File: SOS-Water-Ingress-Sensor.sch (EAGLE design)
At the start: 1 part

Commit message: Update board design and schematic.
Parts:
- added JP1: (no value), SparkFun-Connectors:M03PTH
- added Q1: (no value), SparkFun-DiscreteSemi:TRANSISTOR_PNPSMD
- added R1, R3: 10K, resistor:R-US_R0603
- added R2: 200K, resistor:R-US_R0603
- added U$1, U$2, U$3, U$4: JSH-GH-2VERT, BlueRobotics-JST-GH:JSH-GH-2VERT
- added U$5: JST-GH-3VERT, BlueRobotics-JST-GH:JST-GH-3VERT
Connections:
- new net GND: JP1.1, R3.2, U$1.2, U$2.2, U$3.2, U$4.2
- new net N$1: Q1.B, R1.1, R2.1
- new net PROBE: R1.2, U$1.1, U$2.1, U$3.1, U$4.1
- new net SIGNAL: JP1.3, Q1.C, R3.1
- new net VCC: JP1.2, Q1.E, R2.2
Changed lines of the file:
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@@
 <part name="FRAME1" library="BlueRobotics-Main" deviceset="FRAME-BLUEROBOTICS" device=""/>
 <part name="U$7" library="BR-Eagle-Library" deviceset="LOGO" device="BR-LOGO-S" value="LOGOBR-LOGO-S"/>
+<part name="JP1" library="SparkFun-Connectors" deviceset="M03" device="PTH"/>
+<part name="P+1" library="supply1" deviceset="VCC" device=""/>
+<part name="GND1" library="supply1" deviceset="GND" device=""/>
+<part name="R2" library="resistor" deviceset="R-US_" device="R0603" value="200K"/>
+<part name="GND2" library="supply1" deviceset="GND" device=""/>
+<part name="R1" library="resistor" deviceset="R-US_" device="R0603" value="10K"/>
+<part name="P+2" library="supply1" deviceset="VCC" device=""/>
+<part name="U$1" library="BlueRobotics-JST-GH" deviceset="JSH-GH-2" device="VERT"/>
+<part name="Q1" library="SparkFun-DiscreteSemi" deviceset="TRANSISTOR_PNP" device="SMD"/>
+<part name="R3" library="resistor" deviceset="R-US_" device="R0603" value="10K"/>
+<part name="U$2" library="BlueRobotics-JST-GH" deviceset="JSH-GH-2" device="VERT"/>
+<part name="U$3" library="BlueRobotics-JST-GH" deviceset="JSH-GH-2" device="VERT"/>
+<part name="U$4" library="BlueRobotics-JST-GH" deviceset="JSH-GH-2" device="VERT"/>
+<part name="U$5" library="BlueRobotics-JST-GH" deviceset="JST-GH-3" device="VERT"/>
 </parts>
 <sheets>
@@
 </plain>
 <instances>
-<instance part="FRAME1" gate="G$1" x="-96.52" y="-88.9"/>
-<instance part="FRAME1" gate="G$2" x="50.8" y="-88.9"/>
-<instance part="U$7" gate="G$1" x="127" y="78.74"/>
+<instance part="FRAME1" gate="G$1" x="0" y="0"/>
+<instance part="FRAME1" gate="G$2" x="147.32" y="0"/>
+<instance part="U$7" gate="G$1" x="223.52" y="167.64"/>
+<instance part="JP1" gate="G$1" x="43.18" y="127"/>
+<instance part="P+1" gate="VCC" x="58.42" y="139.7"/>
+<instance part="GND1" gate="1" x="58.42" y="116.84"/>
+<instance part="R2" gate="G$1" x="119.38" y="111.76" rot="R90"/>
+<instance part="GND2" gate="1" x="132.08" y="78.74"/>
+<instance part="R1" gate="G$1" x="109.22" y="104.14" rot="R180"/>
+<instance part="P+2" gate="VCC" x="132.08" y="124.46"/>
+<instance part="U$1" gate="G$1" x="187.96" y="127"/>
+<instance part="Q1" gate="G$1" x="129.54" y="104.14"/>
+<instance part="R3" gate="G$1" x="132.08" y="88.9" rot="R270"/>
+<instance part="U$2" gate="G$1" x="187.96" y="114.3"/>
+<instance part="U$3" gate="G$1" x="187.96" y="101.6"/>
+<instance part="U$4" gate="G$1" x="187.96" y="88.9"/>
+<instance part="U$5" gate="G$1" x="45.72" y="106.68" rot="R180"/>
 </instances>
 <busses>
 </busses>
 <nets>
+<net name="VCC" class="0">
+<segment>
+<pinref part="P+1" gate="VCC" pin="VCC"/>
+<wire x1="58.42" y1="127" x2="58.42" y2="137.16" width="0.1524" layer="91"/>
+<pinref part="JP1" gate="G$1" pin="2"/>
+<wire x1="50.8" y1="127" x2="58.42" y2="127" width="0.1524" layer="91"/>
+</segment>
+<segment>
+<pinref part="P+2" gate="VCC" pin="VCC"/>
+<pinref part="R2" gate="G$1" pin="2"/>
+<wire x1="132.08" y1="119.38" x2="132.08" y2="121.92" width="0.1524" layer="91"/>
+<wire x1="119.38" y1="116.84" x2="119.38" y2="119.38" width="0.1524" layer="91"/>
+<wire x1="119.38" y1="119.38" x2="132.08" y2="119.38" width="0.1524" layer="91"/>
+<junction x="132.08" y="119.38"/>
+<pinref part="Q1" gate="G$1" pin="E"/>
+<wire x1="132.08" y1="109.22" x2="132.08" y2="119.38" width="0.1524" layer="91"/>
+</segment>
+</net>
+<net name="GND" class="0">
+<segment>
+<pinref part="JP1" gate="G$1" pin="1"/>
+<pinref part="GND1" gate="1" pin="GND"/>
+<wire x1="50.8" y1="124.46" x2="58.42" y2="124.46" width="0.1524" layer="91"/>
+<wire x1="58.42" y1="124.46" x2="58.42" y2="119.38" width="0.1524" layer="91"/>
+</segment>
+<segment>
+<pinref part="U$1" gate="G$1" pin="2"/>
+<wire x1="182.88" y1="132.08" x2="180.34" y2="132.08" width="0.1524" layer="91"/>
+<label x="170.18" y="132.08" size="1.778" layer="95"/>
+<pinref part="U$4" gate="G$1" pin="2"/>
+<wire x1="180.34" y1="132.08" x2="170.18" y2="132.08" width="0.1524" layer="91"/>
+<wire x1="182.88" y1="93.98" x2="180.34" y2="93.98" width="0.1524" layer="91"/>
+<wire x1="180.34" y1="93.98" x2="180.34" y2="106.68" width="0.1524" layer="91"/>
+<junction x="180.34" y="132.08"/>
+<pinref part="U$2" gate="G$1" pin="2"/>
+<wire x1="180.34" y1="106.68" x2="180.34" y2="119.38" width="0.1524" layer="91"/>
+<wire x1="180.34" y1="119.38" x2="180.34" y2="132.08" width="0.1524" layer="91"/>
+<wire x1="182.88" y1="119.38" x2="180.34" y2="119.38" width="0.1524" layer="91"/>
+<junction x="180.34" y="119.38"/>
+<pinref part="U$3" gate="G$1" pin="2"/>
+<wire x1="182.88" y1="106.68" x2="180.34" y2="106.68" width="0.1524" layer="91"/>
+<junction x="180.34" y="106.68"/>
+</segment>
+<segment>
+<pinref part="GND2" gate="1" pin="GND"/>
+<pinref part="R3" gate="G$1" pin="2"/>
+<wire x1="132.08" y1="81.28" x2="132.08" y2="83.82" width="0.1524" layer="91"/>
+</segment>
+</net>
+<net name="SIGNAL" class="0">
+<segment>
+<pinref part="JP1" gate="G$1" pin="3"/>
+<wire x1="50.8" y1="129.54" x2="71.12" y2="129.54" width="0.1524" layer="91"/>
+<label x="60.96" y="129.54" size="1.778" layer="95"/>
+</segment>
+<segment>
+<pinref part="Q1" gate="G$1" pin="C"/>
+<pinref part="R3" gate="G$1" pin="1"/>
+<wire x1="132.08" y1="93.98" x2="132.08" y2="96.52" width="0.1524" layer="91"/>
+<wire x1="132.08" y1="96.52" x2="132.08" y2="99.06" width="0.1524" layer="91"/>
+<wire x1="132.08" y1="96.52" x2="147.32" y2="96.52" width="0.1524" layer="91"/>
+<junction x="132.08" y="96.52"/>
+<label x="139.7" y="96.52" size="1.778" layer="95"/>
+</segment>
+</net>
+<net name="N$1" class="0">
+<segment>
+<wire x1="114.3" y1="104.14" x2="119.38" y2="104.14" width="0.1524" layer="91"/>
+<pinref part="R1" gate="G$1" pin="1"/>
+<pinref part="Q1" gate="G$1" pin="B"/>
+<pinref part="R2" gate="G$1" pin="1"/>
+<wire x1="119.38" y1="104.14" x2="127" y2="104.14" width="0.1524" layer="91"/>
+<wire x1="119.38" y1="106.68" x2="119.38" y2="104.14" width="0.1524" layer="91"/>
+<junction x="119.38" y="104.14"/>
+</segment>
+</net>
+<net name="PROBE" class="0">
+<segment>
+<pinref part="U$1" gate="G$1" pin="1"/>
+<wire x1="182.88" y1="129.54" x2="177.8" y2="129.54" width="0.1524" layer="91"/>
+<label x="170.18" y="129.54" size="1.778" layer="95"/>
+<pinref part="U$4" gate="G$1" pin="1"/>
+<wire x1="177.8" y1="129.54" x2="170.18" y2="129.54" width="0.1524" layer="91"/>
+<wire x1="182.88" y1="91.44" x2="177.8" y2="91.44" width="0.1524" layer="91"/>
+<wire x1="177.8" y1="91.44" x2="177.8" y2="104.14" width="0.1524" layer="91"/>
+<junction x="177.8" y="129.54"/>
+<pinref part="U$2" gate="G$1" pin="1"/>
+<wire x1="177.8" y1="104.14" x2="177.8" y2="116.84" width="0.1524" layer="91"/>
+<wire x1="177.8" y1="116.84" x2="177.8" y2="129.54" width="0.1524" layer="91"/>
+<wire x1="182.88" y1="116.84" x2="177.8" y2="116.84" width="0.1524" layer="91"/>
+<junction x="177.8" y="116.84"/>
+<pinref part="U$3" gate="G$1" pin="1"/>
+<wire x1="182.88" y1="104.14" x2="177.8" y2="104.14" width="0.1524" layer="91"/>
+<junction x="177.8" y="104.14"/>
+</segment>
+<segment>
+<pinref part="R1" gate="G$1" pin="2"/>
+<wire x1="104.14" y1="104.14" x2="93.98" y2="104.14" width="0.1524" layer="91"/>
+<label x="93.98" y="104.14" size="1.778" layer="95"/>
+</segment>
+</net>
 </nets>
 </sheet>

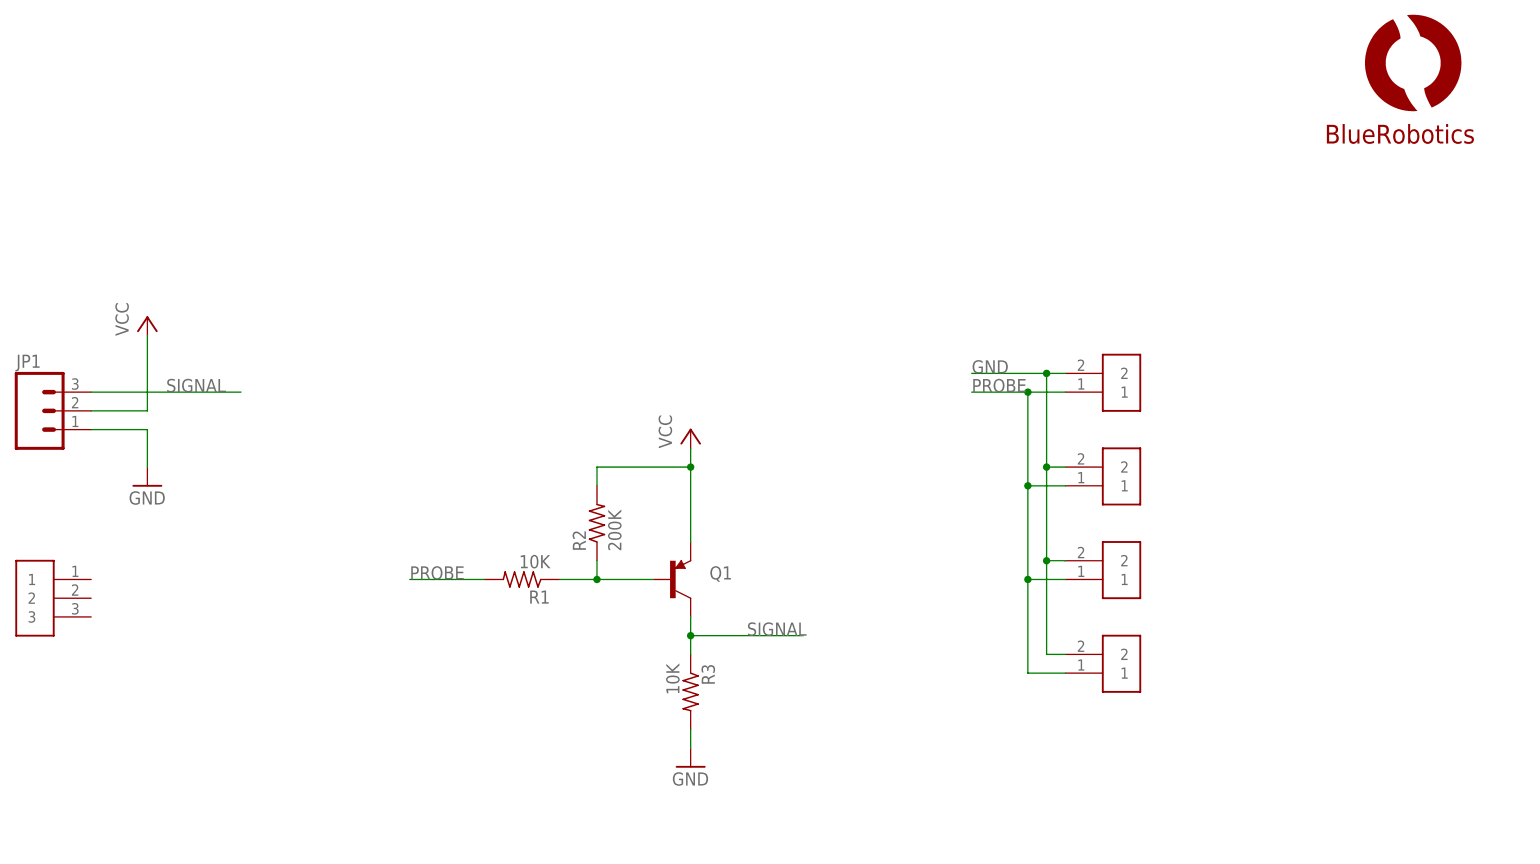
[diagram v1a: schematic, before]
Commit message: Added LED indicator and resistor, completed board layout.
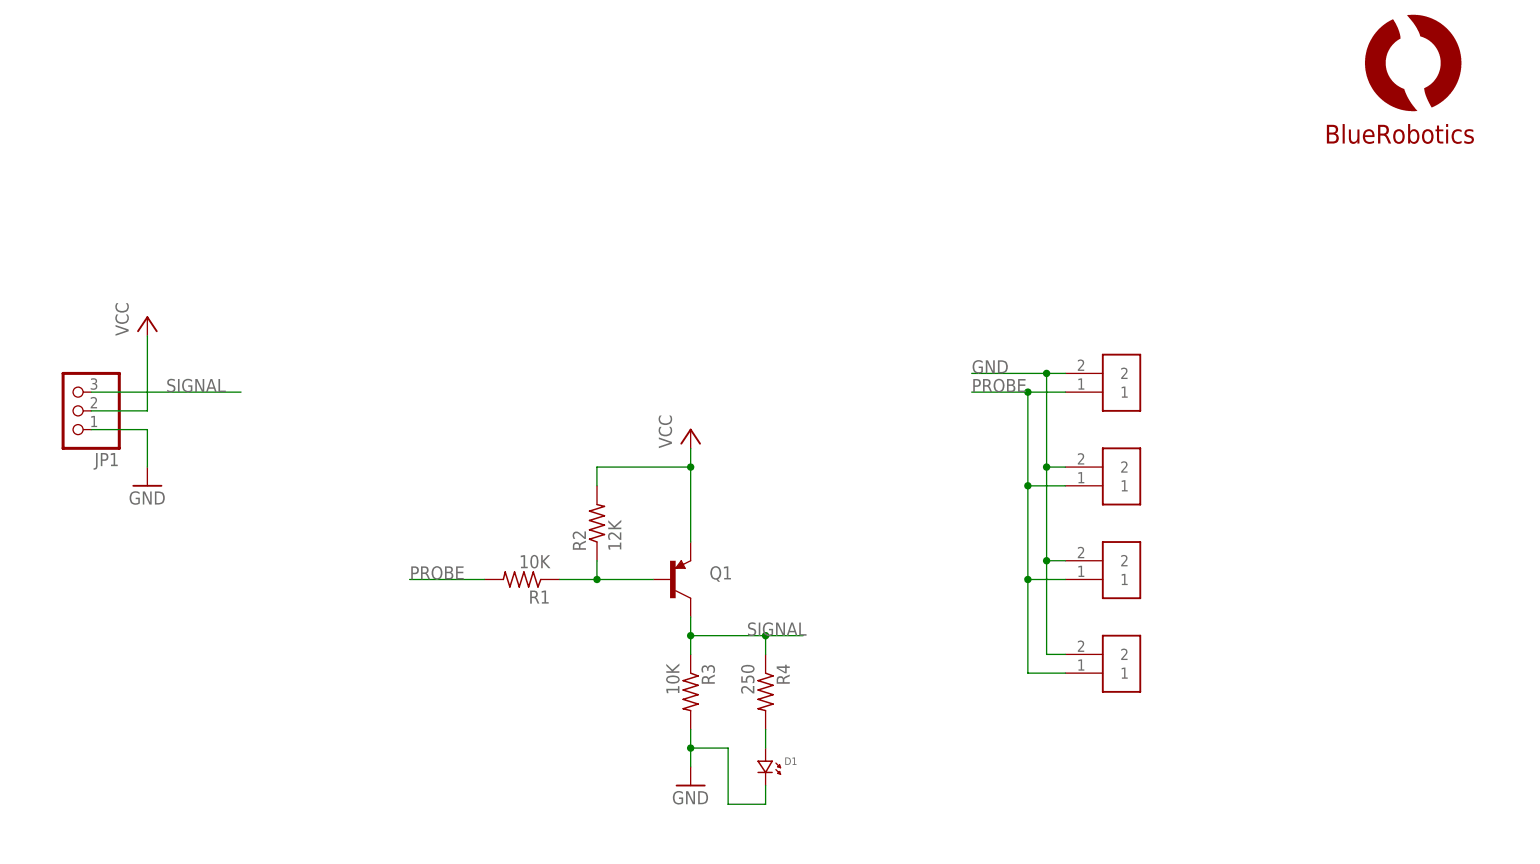
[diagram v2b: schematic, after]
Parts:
- removed U$5: JST-GH-3VERT, BlueRobotics-JST-GH:JST-GH-3VERT
- added D1: (no value), standardparts:LED.0805
- added R4: 250, resistor:R-US_R0603
- JP1: device SparkFun-Connectors:M03PTH -> pinhead+:PINHD-1X3
- R2: value 200K -> 12K
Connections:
- new net N$2: D1.1, R4.2
- net GND: now also D1.2
- net SIGNAL: now also R4.1
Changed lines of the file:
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@@
 <?xml version="1.0" encoding="utf-8"?>
 <!DOCTYPE eagle SYSTEM "eagle.dtd">
-<eagle version="7.4.0">
+<eagle version="7.6.0">
 <drawing>
 <settings>
@@
 <layer number="56" name="wert" color="7" fill="1" visible="no" active="no"/>
 <layer number="57" name="tCAD" color="7" fill="1" visible="no" active="no"/>
+<layer number="59" name="tCarbon" color="7" fill="1" visible="no" active="no"/>
+<layer number="60" name="bCarbon" color="7" fill="1" visible="no" active="no"/>
 <layer number="90" name="Modules" color="5" fill="1" visible="yes" active="yes"/>
 <layer number="91" name="Nets" color="2" fill="1" visible="yes" active="yes"/>
@@
 <layer number="127" name="_tValues" color="7" fill="1" visible="yes" active="yes"/>
 <layer number="128" name="_bValues" color="7" fill="1" visible="yes" active="yes"/>
+<layer number="129" name="Mask" color="7" fill="1" visible="yes" active="yes"/>
 <layer number="130" name="SMDSTROOK" color="7" fill="1" visible="yes" active="yes"/>
 <layer number="131" name="tAdjust" color="7" fill="1" visible="yes" active="yes"/>
@@
 <layer number="227" name="227bmp" color="7" fill="1" visible="yes" active="yes"/>
 <layer number="228" name="228bmp" color="7" fill="1" visible="yes" active="yes"/>
+<layer number="229" name="229bmp" color="7" fill="1" visible="yes" active="yes"/>
 <layer number="230" name="230bmp" color="7" fill="1" visible="yes" active="yes"/>
 <layer number="231" name="Eagle3D_PG1" color="7" fill="1" visible="yes" active="yes"/>
@@
 <part name="FRAME1" library="BlueRobotics-Main" deviceset="FRAME-BLUEROBOTICS" device=""/>
 <part name="U$7" library="BR-Eagle-Library" deviceset="LOGO" device="BR-LOGO-S" value="LOGOBR-LOGO-S"/>
-<part name="JP1" library="SparkFun-Connectors" deviceset="M03" device="PTH"/>
 <part name="P+1" library="supply1" deviceset="VCC" device=""/>
 <part name="GND1" library="supply1" deviceset="GND" device=""/>
-<part name="R2" library="resistor" deviceset="R-US_" device="R0603" value="200K"/>
+<part name="R2" library="resistor" deviceset="R-US_" device="R0603" value="12K"/>
 <part name="GND2" library="supply1" deviceset="GND" device=""/>
 <part name="R1" library="resistor" deviceset="R-US_" device="R0603" value="10K"/>
@@
 <part name="U$2" library="BlueRobotics-JST-GH" deviceset="JSH-GH-2" device="VERT"/>
 <part name="U$3" library="BlueRobotics-JST-GH" deviceset="JSH-GH-2" device="VERT"/>
+<part name="JP1" library="pinhead+" deviceset="PINHD-1X3" device=""/>
+<part name="R4" library="resistor" deviceset="R-US_" device="R0603" value="250"/>
+<part name="D1" library="standardparts" deviceset="LED" device=".0805"/>
 <part name="U$4" library="BlueRobotics-JST-GH" deviceset="JSH-GH-2" device="VERT"/>
-<part name="U$5" library="BlueRobotics-JST-GH" deviceset="JST-GH-3" device="VERT"/>
 </parts>
 <sheets>
@@
 <instance part="FRAME1" gate="G$2" x="147.32" y="0"/>
 <instance part="U$7" gate="G$1" x="223.52" y="167.64"/>
-<instance part="JP1" gate="G$1" x="43.18" y="127"/>
 <instance part="P+1" gate="VCC" x="58.42" y="139.7"/>
 <instance part="GND1" gate="1" x="58.42" y="116.84"/>
 <instance part="R2" gate="G$1" x="119.38" y="111.76" rot="R90"/>
-<instance part="GND2" gate="1" x="132.08" y="78.74"/>
+<instance part="GND2" gate="1" x="132.08" y="76.2"/>
 <instance part="R1" gate="G$1" x="109.22" y="104.14" rot="R180"/>
 <instance part="P+2" gate="VCC" x="132.08" y="124.46"/>
@@
 <instance part="U$2" gate="G$1" x="187.96" y="114.3"/>
 <instance part="U$3" gate="G$1" x="187.96" y="101.6"/>
+<instance part="JP1" gate="A" x="48.26" y="127" rot="R180"/>
+<instance part="R4" gate="G$1" x="142.24" y="88.9" rot="R270"/>
+<instance part="D1" gate="G$1" x="142.24" y="78.74" rot="R270"/>
 <instance part="U$4" gate="G$1" x="187.96" y="88.9"/>
-<instance part="U$5" gate="G$1" x="45.72" y="106.68" rot="R180"/>
 </instances>
 <busses>
@@
 <pinref part="P+1" gate="VCC" pin="VCC"/>
 <wire x1="58.42" y1="127" x2="58.42" y2="137.16" width="0.1524" layer="91"/>
-<pinref part="JP1" gate="G$1" pin="2"/>
 <wire x1="50.8" y1="127" x2="58.42" y2="127" width="0.1524" layer="91"/>
+<pinref part="JP1" gate="A" pin="2"/>
 </segment>
 <segment>
@@
 <net name="GND" class="0">
 <segment>
-<pinref part="JP1" gate="G$1" pin="1"/>
 <pinref part="GND1" gate="1" pin="GND"/>
 <wire x1="50.8" y1="124.46" x2="58.42" y2="124.46" width="0.1524" layer="91"/>
 <wire x1="58.42" y1="124.46" x2="58.42" y2="119.38" width="0.1524" layer="91"/>
+<pinref part="JP1" gate="A" pin="1"/>
 </segment>
 <segment>
@@
 <wire x1="182.88" y1="132.08" x2="180.34" y2="132.08" width="0.1524" layer="91"/>
 <label x="170.18" y="132.08" size="1.778" layer="95"/>
-<pinref part="U$4" gate="G$1" pin="2"/>
 <wire x1="180.34" y1="132.08" x2="170.18" y2="132.08" width="0.1524" layer="91"/>
-<wire x1="182.88" y1="93.98" x2="180.34" y2="93.98" width="0.1524" layer="91"/>
-<wire x1="180.34" y1="93.98" x2="180.34" y2="106.68" width="0.1524" layer="91"/>
 <junction x="180.34" y="132.08"/>
 <pinref part="U$2" gate="G$1" pin="2"/>
@@
 <pinref part="U$3" gate="G$1" pin="2"/>
 <wire x1="182.88" y1="106.68" x2="180.34" y2="106.68" width="0.1524" layer="91"/>
+<wire x1="180.34" y1="106.68" x2="180.34" y2="93.98" width="0.1524" layer="91"/>
 <junction x="180.34" y="106.68"/>
+<pinref part="U$4" gate="G$1" pin="2"/>
+<wire x1="180.34" y1="93.98" x2="182.88" y2="93.98" width="0.1524" layer="91"/>
 </segment>
 <segment>
 <pinref part="GND2" gate="1" pin="GND"/>
 <pinref part="R3" gate="G$1" pin="2"/>
+<wire x1="132.08" y1="78.74" x2="132.08" y2="81.28" width="0.1524" layer="91"/>
+<pinref part="D1" gate="G$1" pin="2"/>
 <wire x1="132.08" y1="81.28" x2="132.08" y2="83.82" width="0.1524" layer="91"/>
+<wire x1="142.24" y1="76.2" x2="142.24" y2="73.66" width="0.1524" layer="91"/>
+<wire x1="142.24" y1="73.66" x2="137.16" y2="73.66" width="0.1524" layer="91"/>
+<wire x1="137.16" y1="73.66" x2="137.16" y2="81.28" width="0.1524" layer="91"/>
+<wire x1="137.16" y1="81.28" x2="132.08" y2="81.28" width="0.1524" layer="91"/>
+<junction x="132.08" y="81.28"/>
 </segment>
 </net>
 <net name="SIGNAL" class="0">
 <segment>
-<pinref part="JP1" gate="G$1" pin="3"/>
 <wire x1="50.8" y1="129.54" x2="71.12" y2="129.54" width="0.1524" layer="91"/>
 <label x="60.96" y="129.54" size="1.778" layer="95"/>
+<pinref part="JP1" gate="A" pin="3"/>
 </segment>
 <segment>
@@
 <wire x1="132.08" y1="93.98" x2="132.08" y2="96.52" width="0.1524" layer="91"/>
 <wire x1="132.08" y1="96.52" x2="132.08" y2="99.06" width="0.1524" layer="91"/>
-<wire x1="132.08" y1="96.52" x2="147.32" y2="96.52" width="0.1524" layer="91"/>
+<wire x1="132.08" y1="96.52" x2="142.24" y2="96.52" width="0.1524" layer="91"/>
 <junction x="132.08" y="96.52"/>
 <label x="139.7" y="96.52" size="1.778" layer="95"/>
+<pinref part="R4" gate="G$1" pin="1"/>
+<wire x1="142.24" y1="96.52" x2="147.32" y2="96.52" width="0.1524" layer="91"/>
+<wire x1="142.24" y1="96.52" x2="142.24" y2="93.98" width="0.1524" layer="91"/>
+<junction x="142.24" y="96.52"/>
 </segment>
 </net>
@@
 <wire x1="182.88" y1="129.54" x2="177.8" y2="129.54" width="0.1524" layer="91"/>
 <label x="170.18" y="129.54" size="1.778" layer="95"/>
-<pinref part="U$4" gate="G$1" pin="1"/>
 <wire x1="177.8" y1="129.54" x2="170.18" y2="129.54" width="0.1524" layer="91"/>
-<wire x1="182.88" y1="91.44" x2="177.8" y2="91.44" width="0.1524" layer="91"/>
-<wire x1="177.8" y1="91.44" x2="177.8" y2="104.14" width="0.1524" layer="91"/>
 <junction x="177.8" y="129.54"/>
 <pinref part="U$2" gate="G$1" pin="1"/>
@@
 <pinref part="U$3" gate="G$1" pin="1"/>
 <wire x1="182.88" y1="104.14" x2="177.8" y2="104.14" width="0.1524" layer="91"/>
+<wire x1="177.8" y1="104.14" x2="177.8" y2="91.44" width="0.1524" layer="91"/>
 <junction x="177.8" y="104.14"/>
+<pinref part="U$4" gate="G$1" pin="1"/>
+<wire x1="177.8" y1="91.44" x2="182.88" y2="91.44" width="0.1524" layer="91"/>
 </segment>
 <segment>
@@
 </segment>
 </net>
+<net name="N$2" class="0">
+<segment>
+<pinref part="R4" gate="G$1" pin="2"/>
+<wire x1="142.24" y1="83.82" x2="142.24" y2="81.28" width="0.1524" layer="91"/>
+<pinref part="D1" gate="G$1" pin="1"/>
+</segment>
+</net>
